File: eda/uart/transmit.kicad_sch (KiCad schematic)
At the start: 6 parts, among them U1 74HCT193, U2 74HCT165, U3 74HCT165

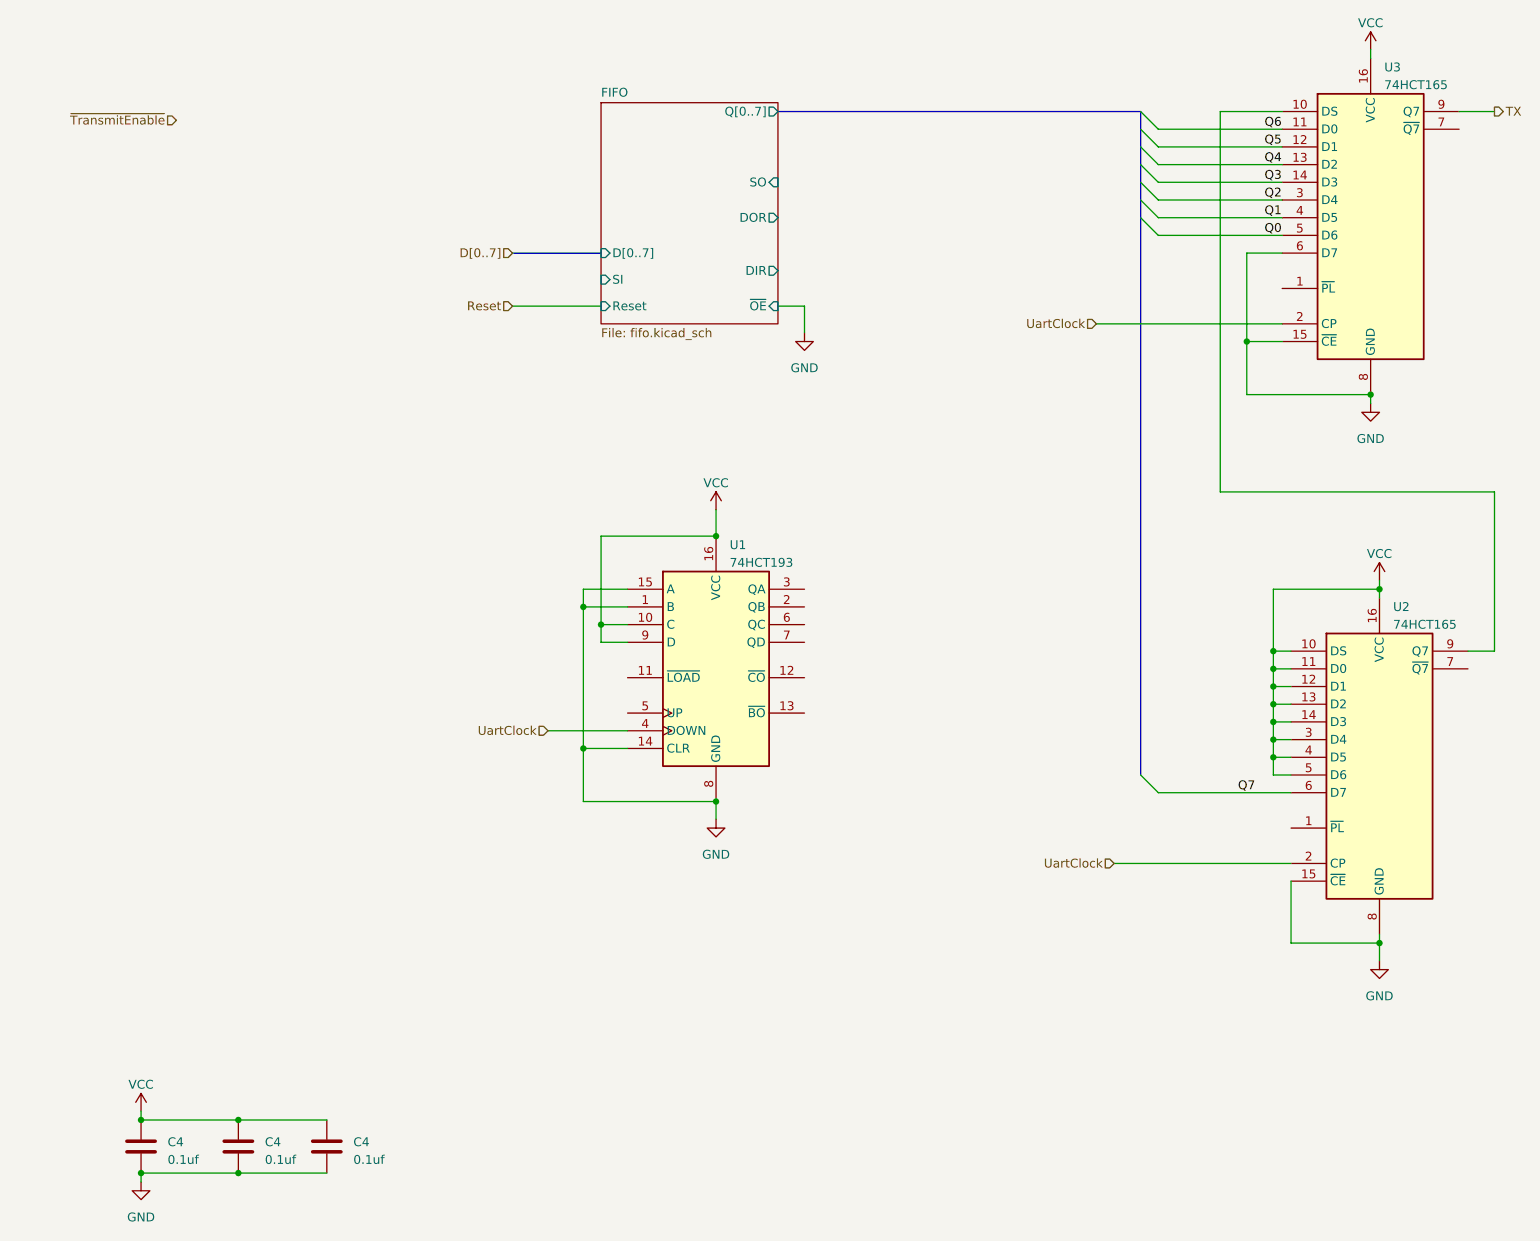
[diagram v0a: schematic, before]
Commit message: Port main board schematic to kicad
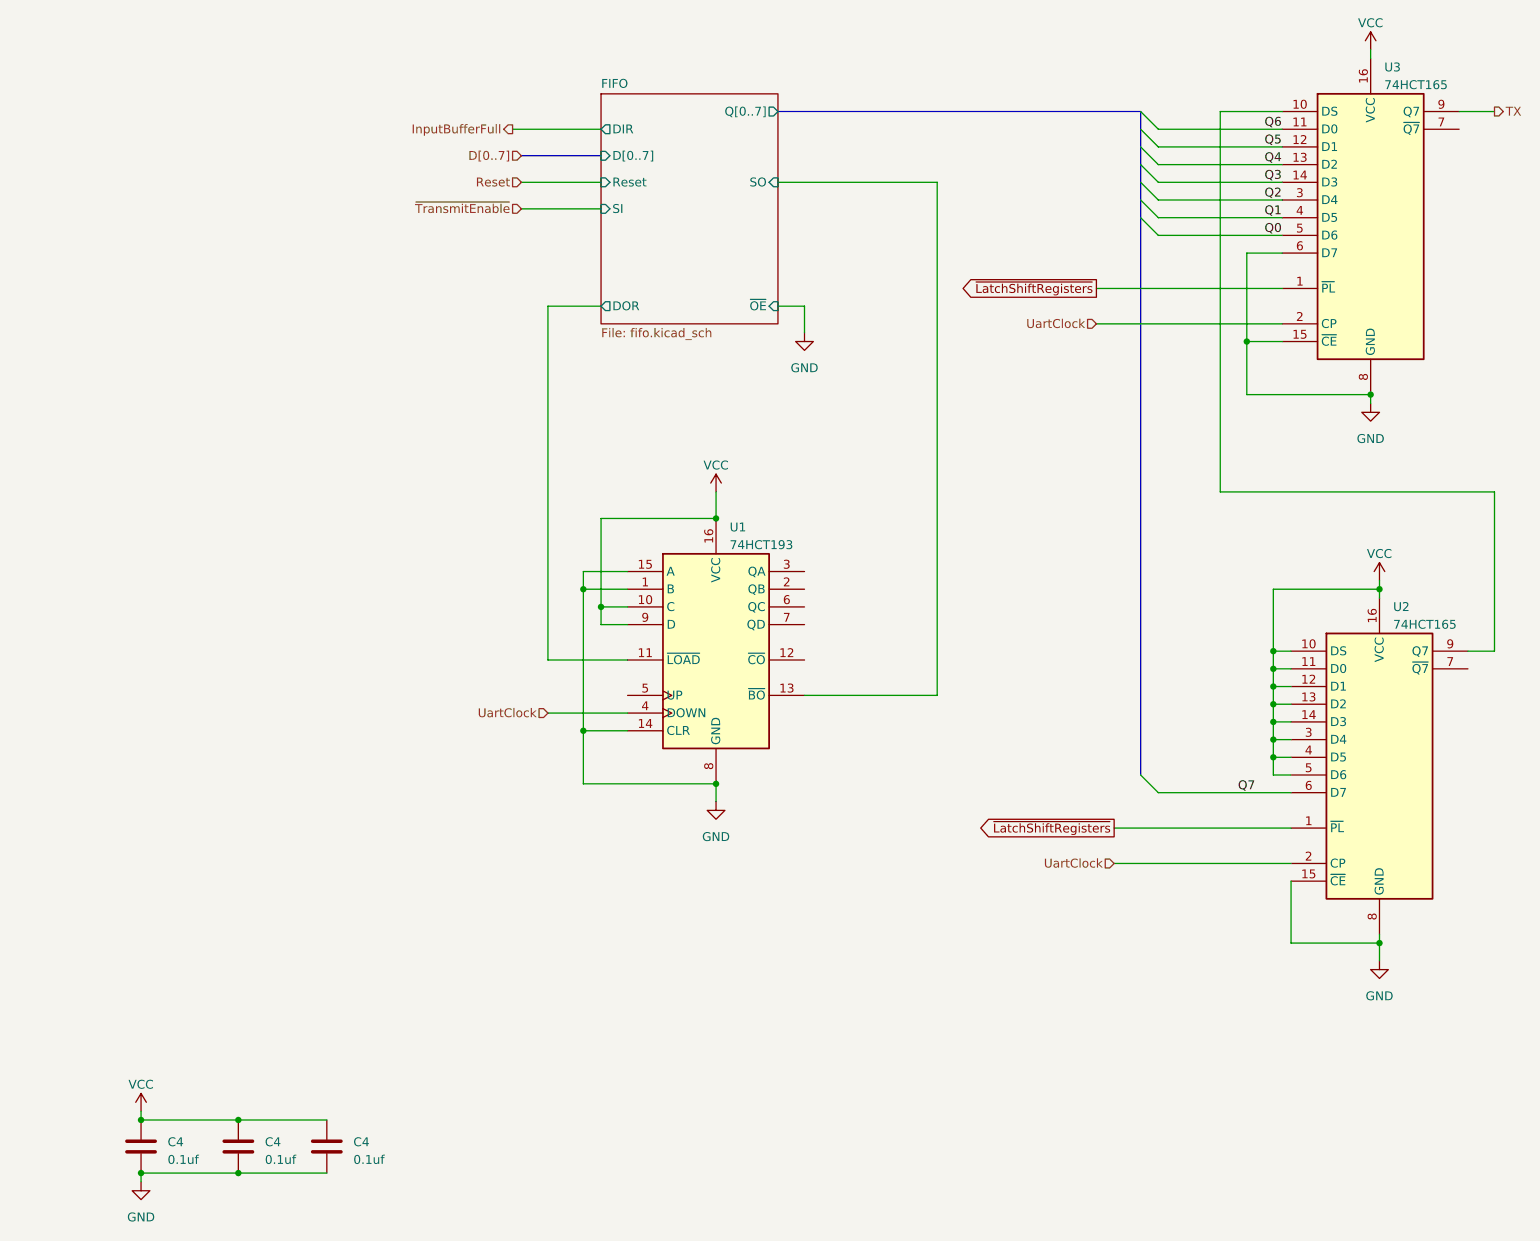
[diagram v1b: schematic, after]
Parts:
- C4: footprint Capacitor_THT:C_Rect_L7.2mm_W2.5mm_P5.00mm_FKS2_FKP2_MKS2_MKP2 -> Capacitor_THT:C_Rect_L7.2mm_W3.5mm_P5.00mm_FKS2_FKP2_MKS2_MKP2
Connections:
- net FIFO/DOR: now also U1.11 (~{LOAD})
- net FIFO/SO: now also U1.13 (~{BO})
- net ~{LatchShiftRegisters}: now reaches U2.1 (~{PL})
- net ~{LatchShiftRegisters}: now also U3.1 (~{PL})
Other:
- moved on the sheet: U1

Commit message: Work on main board eda, interim
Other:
- sheet FIFO renamed FIFO Transmit
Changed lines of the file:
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@@
     (stroke (width 0) (type default))
   )
-  (label "Q1" (at 196.85 48.26 0)
-    (effects (font (size 1.27 1.27)) (justify left bottom))
-  )
-  (label "Q6" (at 196.85 35.56 0)
-    (effects (font (size 1.27 1.27)) (justify left bottom))
-  )
-  (label "Q2" (at 196.85 45.72 0)
-    (effects (font (size 1.27 1.27)) (justify left bottom))
-  )
-  (label "Q4" (at 196.85 40.64 0)
-    (effects (font (size 1.27 1.27)) (justify left bottom))
-  )
-  (label "Q0" (at 196.85 50.8 0)
-    (effects (font (size 1.27 1.27)) (justify left bottom))
-  )
-  (label "Q5" (at 196.85 38.1 0)
-    (effects (font (size 1.27 1.27)) (justify left bottom))
-  )
-  (label "Q3" (at 196.85 43.18 0)
-    (effects (font (size 1.27 1.27)) (justify left bottom))
-  )
-  (label "Q7" (at 193.04 130.81 0)
+  (label "Q1" (at 196.85 48.26 0) (fields_autoplaced)
+    (effects (font (size 1.27 1.27)) (justify left bottom))
+  )
+  (label "Q6" (at 196.85 35.56 0) (fields_autoplaced)
+    (effects (font (size 1.27 1.27)) (justify left bottom))
+  )
+  (label "Q2" (at 196.85 45.72 0) (fields_autoplaced)
+    (effects (font (size 1.27 1.27)) (justify left bottom))
+  )
+  (label "Q4" (at 196.85 40.64 0) (fields_autoplaced)
+    (effects (font (size 1.27 1.27)) (justify left bottom))
+  )
+  (label "Q0" (at 196.85 50.8 0) (fields_autoplaced)
+    (effects (font (size 1.27 1.27)) (justify left bottom))
+  )
+  (label "Q5" (at 196.85 38.1 0) (fields_autoplaced)
+    (effects (font (size 1.27 1.27)) (justify left bottom))
+  )
+  (label "Q3" (at 196.85 43.18 0) (fields_autoplaced)
+    (effects (font (size 1.27 1.27)) (justify left bottom))
+  )
+  (label "Q7" (at 193.04 130.81 0) (fields_autoplaced)
     (effects (font (size 1.27 1.27)) (justify left bottom))
   )
@@
     (stroke (width 0.1524) (type solid))
     (fill (color 0 0 0 0.0000))
-    (property "Sheetname" "FIFO" (at 101.6 29.7684 0)
+    (property "Sheetname" "FIFO Transmit" (at 101.6 29.7684 0)
       (effects (font (size 1.27 1.27)) (justify left bottom))
     )

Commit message: Update eda
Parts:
- added U16: 74HCT139, Package_DIP:DIP-16_W7.62mm, symbol 74xx:74LS139
- added U2: 74HCT14, Package_DIP:DIP-14_W7.62mm, symbol 74xx:74LS14
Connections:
- net GND: now also U3.5 (D6); no longer U3.6 (D7)
- net Q0: now also U3.4 (D5); no longer U3.5 (D6)
- net Q1: now also U3.3 (D4); no longer U3.4 (D5)
- net Q2: now also U3.14 (D3); no longer U3.3 (D4)
- net Q3: now also U3.13 (D2); no longer U3.14 (D3)
- net Q4: now also U3.12 (D1); no longer U3.13 (D2)
- net Q5: now also U3.11 (D0); no longer U3.12 (D1)
- net Q6: now also U2.6 (D7); no longer U3.11 (D0)
- net Q7: now also U2.5 (D6); no longer U2.6 (D7)
- net VCC: now also U1.5 (UP), U3.6 (D7); no longer U2.5 (D6)
- net ~{LatchShiftRegisters}: now also U16.9 (O3)
- net at U1.2 (QB): now also U16.14 (A0)
- net at U1.3 (QA): now also U16.13 (A1)
- net at U1.7 (QD): now also U2.1
- new net: U16.15 (E), U2.2
- no-connect marks 0 -> 5
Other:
- moved on the sheet: U1

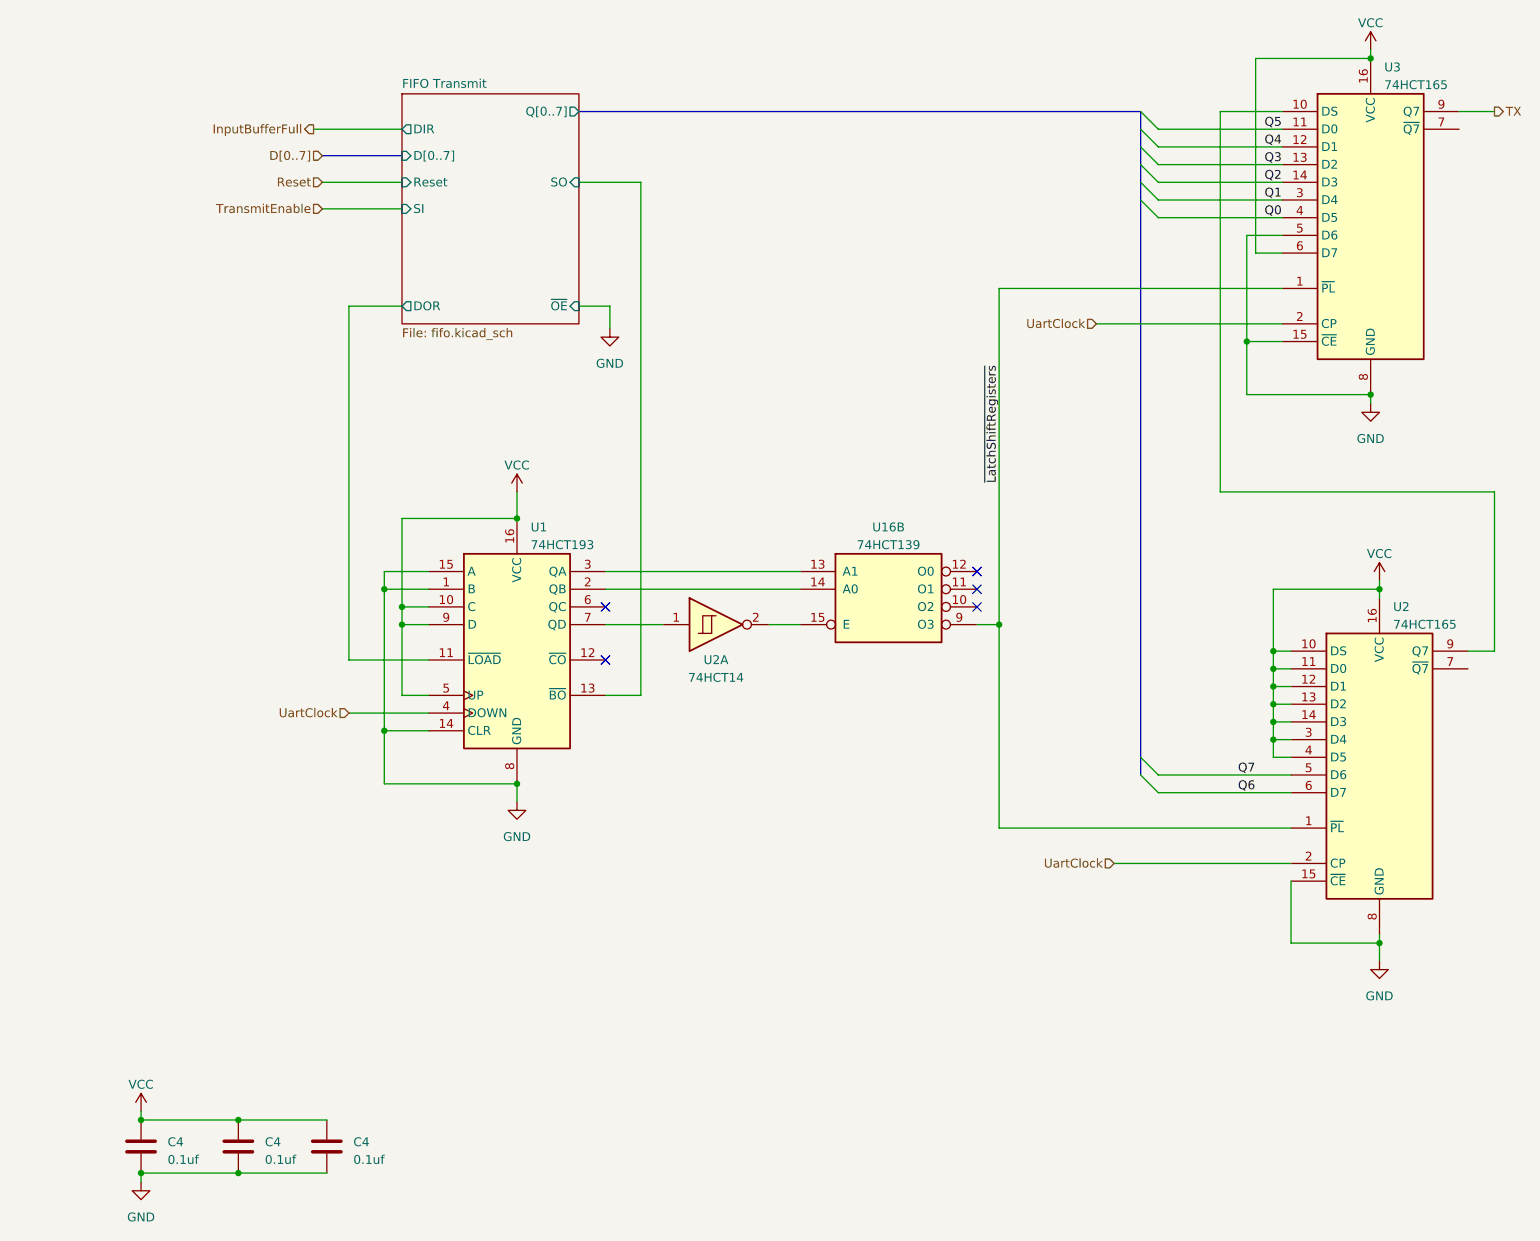
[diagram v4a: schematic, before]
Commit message: Update UART transmit logic
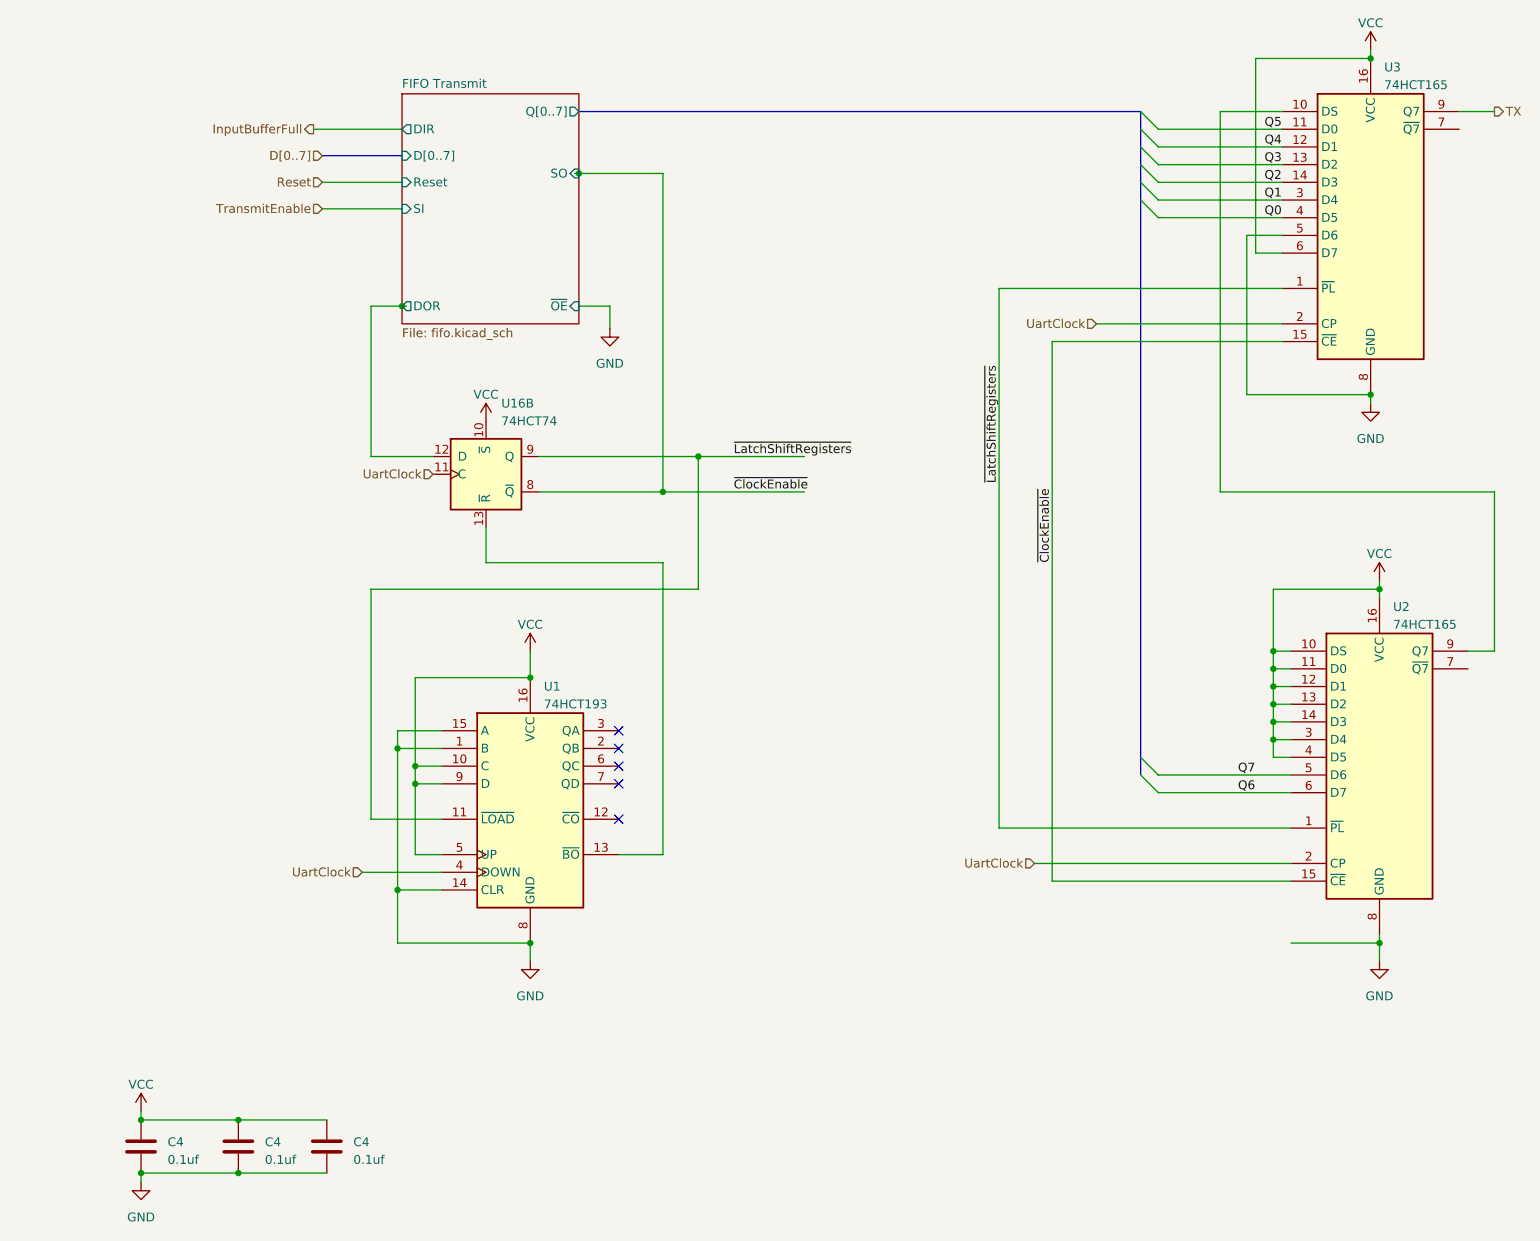
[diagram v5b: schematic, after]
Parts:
- removed U16: 74HCT139, Package_DIP:DIP-16_W7.62mm, symbol 74xx:74LS139
- removed U2: 74HCT14, Package_DIP:DIP-14_W7.62mm, symbol 74xx:74LS14
- added U16: 74HCT74, Package_DIP:DIP-14_W10.16mm, symbol 74xx:74LS74
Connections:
- net FIFO Transmit/DOR: now also U16.12 (D); no longer U1.11 (~{LOAD})
- net GND: no longer U2.15 (~{CE}), U3.15 (~{CE})
- net UartClock: now also U16.11 (C)
- net VCC: now also U16.10 (~{S})
- net ~{LatchShiftRegisters}: now also U1.11 (~{LOAD}), U16.9 (Q)
- net FIFO Transmit/SO: no longer names the net of U1.13 (~{BO})
- net FIFO Transmit/SO: now also U16.13 (~{R})
- new net ~{ClockEnable}: U16.8 (~{Q}), U2.15 (~{CE}), U3.15 (~{CE})
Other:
- moved on the sheet: U1

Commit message: Sync
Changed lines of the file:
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@@
   (symbol (lib_id "74xx:74LS74") (at 85.09 85.09 0) (unit 2)
     (in_bom yes) (on_board yes) (dnp no) (fields_autoplaced)
-    (property "Reference" "U16" (at 87.2841 74.93 0)
+    (property "Reference" "U16" (at 87.0459 76.2 0)
       (effects (font (size 1.27 1.27)) (justify left))
     )
-    (property "Value" "74HCT74" (at 87.2841 77.47 0)
+    (property "Value" "74HCT74" (at 87.0459 78.74 0)
       (effects (font (size 1.27 1.27)) (justify left))
     )
@@
         )
         (path "/11545594-d6d6-4b37-a578-fa23933d5773/58e4c198-6a2b-4c28-a1a8-589b85574c34"
-          (reference "U16") (unit 2)
+          (reference "U16") (unit 1)
         )
       )

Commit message: Branch of uart to v1
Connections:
- no-connect marks 5 -> 6
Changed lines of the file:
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@@
   )
   (no_connect (at 104.14 134.62))
+  (no_connect (at 224.79 35.56))
   (no_connect (at 104.14 124.46))
   (no_connect (at 104.14 121.92))

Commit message: Normalize cap size
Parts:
- C4: footprint Capacitor_THT:C_Rect_L7.2mm_W3.5mm_P5.00mm_FKS2_FKP2_MKS2_MKP2 -> Capacitor_THT:C_Disc_D3.8mm_W2.6mm_P2.50mm
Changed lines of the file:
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@@
       (effects (font (size 1.27 1.27)) (justify left))
     )
-    (property "Footprint" "Capacitor_THT:C_Rect_L7.2mm_W3.5mm_P5.00mm_FKS2_FKP2_MKS2_MKP2" (at 63.1952 185.42 0)
+    (property "Footprint" "Capacitor_THT:C_Disc_D3.8mm_W2.6mm_P2.50mm" (at 63.1952 185.42 0)
       (effects (font (size 1.27 1.27)) hide)
     )
@@
       (effects (font (size 1.27 1.27)) (justify left))
     )
-    (property "Footprint" "Capacitor_THT:C_Rect_L7.2mm_W3.5mm_P5.00mm_FKS2_FKP2_MKS2_MKP2" (at 36.5252 185.42 0)
+    (property "Footprint" "Capacitor_THT:C_Disc_D3.8mm_W2.6mm_P2.50mm" (at 36.5252 185.42 0)
       (effects (font (size 1.27 1.27)) hide)
     )
@@
       (effects (font (size 1.27 1.27)) (justify left))
     )
-    (property "Footprint" "Capacitor_THT:C_Rect_L7.2mm_W3.5mm_P5.00mm_FKS2_FKP2_MKS2_MKP2" (at 50.4952 185.42 0)
-      (effects (font (size 1.27 1.27)) hide)
-    )
+    (property "Footprint" "Capacitor_THT:C_Disc_D3.8mm_W2.6mm_P2.50mm" (at 50.4952 185.42 0)
+      (effects (font (size 1.27 1.27)) hide)
+    )
